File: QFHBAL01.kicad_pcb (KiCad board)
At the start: 2 copper layers, 39.4 x 39.4 mm, 13 parts, among them J1 Conn_Coaxial, T1 Transformer_1P_SS

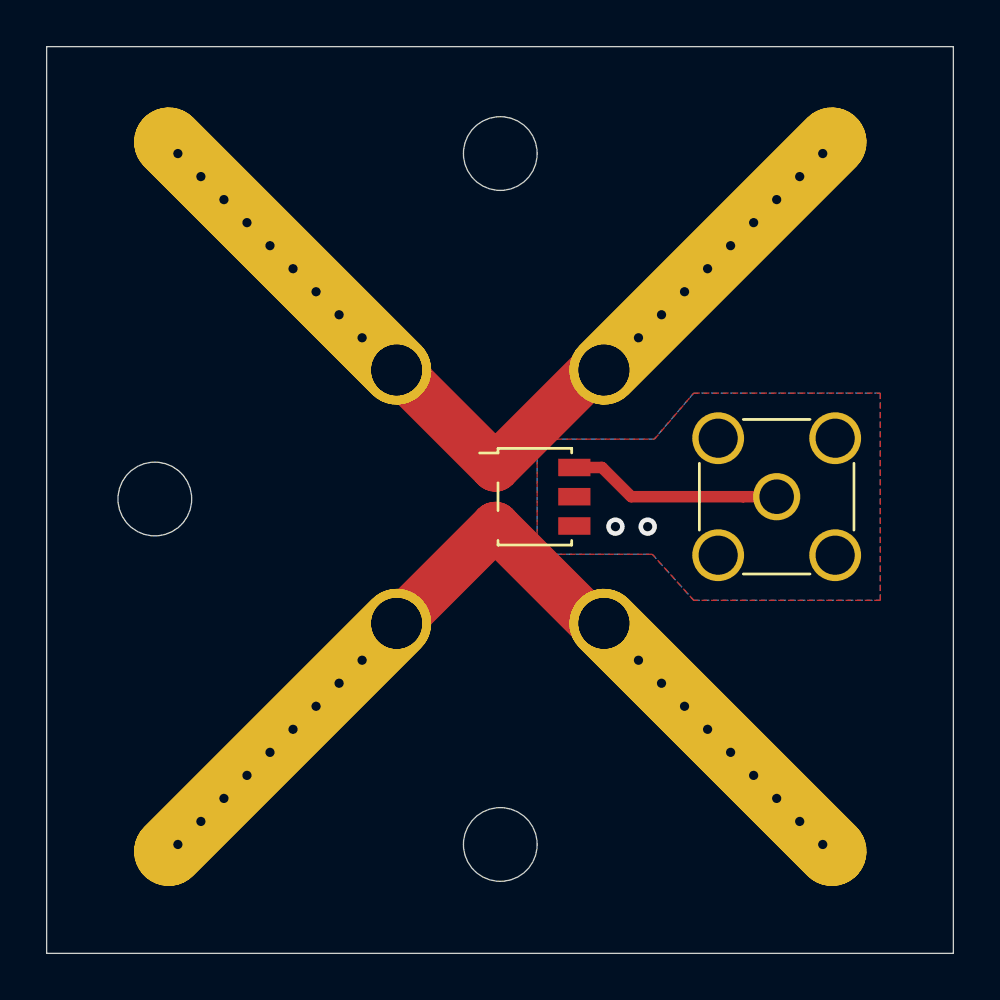
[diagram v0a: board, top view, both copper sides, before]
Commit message: Solved issue #1: Layout upraven pro moznost zapojeni jako "common mode" a "trafo".
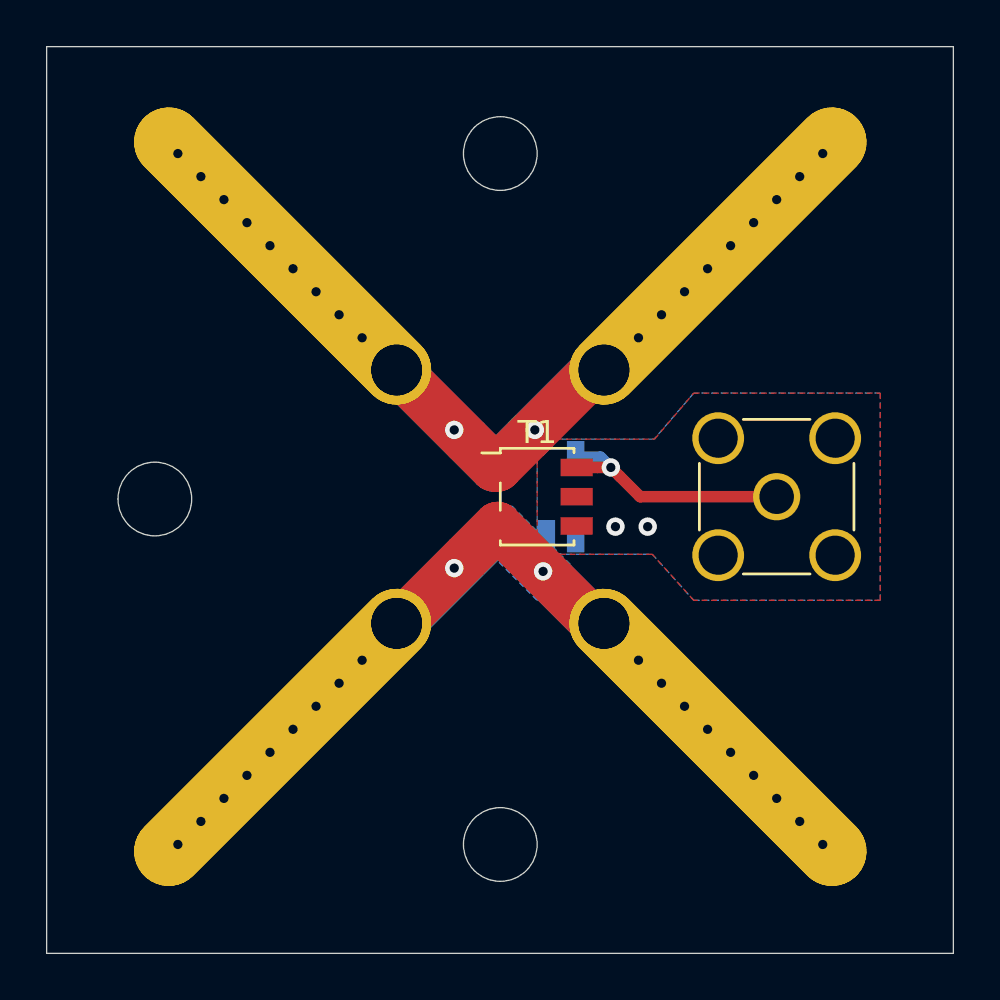
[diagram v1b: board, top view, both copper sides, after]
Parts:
- removed the H2 at (145.5, 84.4) (x2)
- removed the H4 at (154.5, 95.4)
- added H2: Pad, MountingHole:MountingHole_2.2mm_M2_Pad, B.Cu at (145.5, 95.4)
- added H6: Pad, MountingHole:MountingHole_2.2mm_M2_Pad, F.Cu at (154.5, 95.4)
- added H8: Pad, MountingHole:MountingHole_2.2mm_M2_Pad, B.Cu at (154.5, 95.4)
- added T2: ETC1-1-13, Transformer_SMD:Transformer_MACOM_SM-22, B.Cu at (152.0, 89.9)
- H1: renamed from H2; value MountingHole_Pad -> Pad
- H3: renamed from H1; value MountingHole_Pad -> Pad
- H4: value MountingHole_Pad -> Pad; moved to B.Cu
- H5: renamed from H3; value MountingHole_Pad -> Pad
- H7: renamed from H4; value MountingHole_Pad -> Pad
- T1: value Transformer_1P_SS -> ETC1-1-13
- moved H5 14.2 mm to (145.5, 84.4), turned to 0 degrees
- moved H7 11.0 mm to (145.5, 84.4), turned to 270 degrees
- moved T1 0.10 mm to (151.6, 89.9)
- turned H4 to 0 degrees
- renumbered H6 to H10, H8 to H11, H5 to H9
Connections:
- net Net-(J1-Pad1) renamed /OUT
- H1 pad 1: Net-(H1-Pad1) -> /IN1
- H3 pad 1: Net-(H1-Pad1) -> /IN1
- H4 pad 1: Net-(H3-Pad1) -> /IN2
- H5 pad 1: Net-(H3-Pad1) -> /IN1
- H7 pad 1: Net-(H3-Pad1) -> /IN1
- T1 pad 1: Net-(H1-Pad1) -> /IN1
- T1 pad 2: Net-(H3-Pad1) -> /IN2
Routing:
- net /IN1: track 0.00 -> 24.3 mm, vias 0 -> 20
- net /IN2: track 0.00 -> 21.8 mm, vias 0 -> 20
- net Net-(H3-Pad1): track 12.5 -> 0.00 mm, vias 18 -> 0
- net Net-(H1-Pad1): track 12.5 -> 0.00 mm, vias 18 -> 0
- net /OUT: track 9.31 -> 11.0 mm, vias 0 -> 1
- added copper zone on B.Cu, net /IN2

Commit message: Updated to the new version of KiCAD.
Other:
- net class Default removed
